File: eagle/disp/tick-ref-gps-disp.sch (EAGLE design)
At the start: 51 parts, among them CN1 1PPS Out, CN2 ISP, CN3 RS232, CN4 Power In, CN5 Serial Program, U1 ATMEGA168-AU, U2 AS1115, U3 MAX232, U4 LM2931_FIXED, X1 16MHz

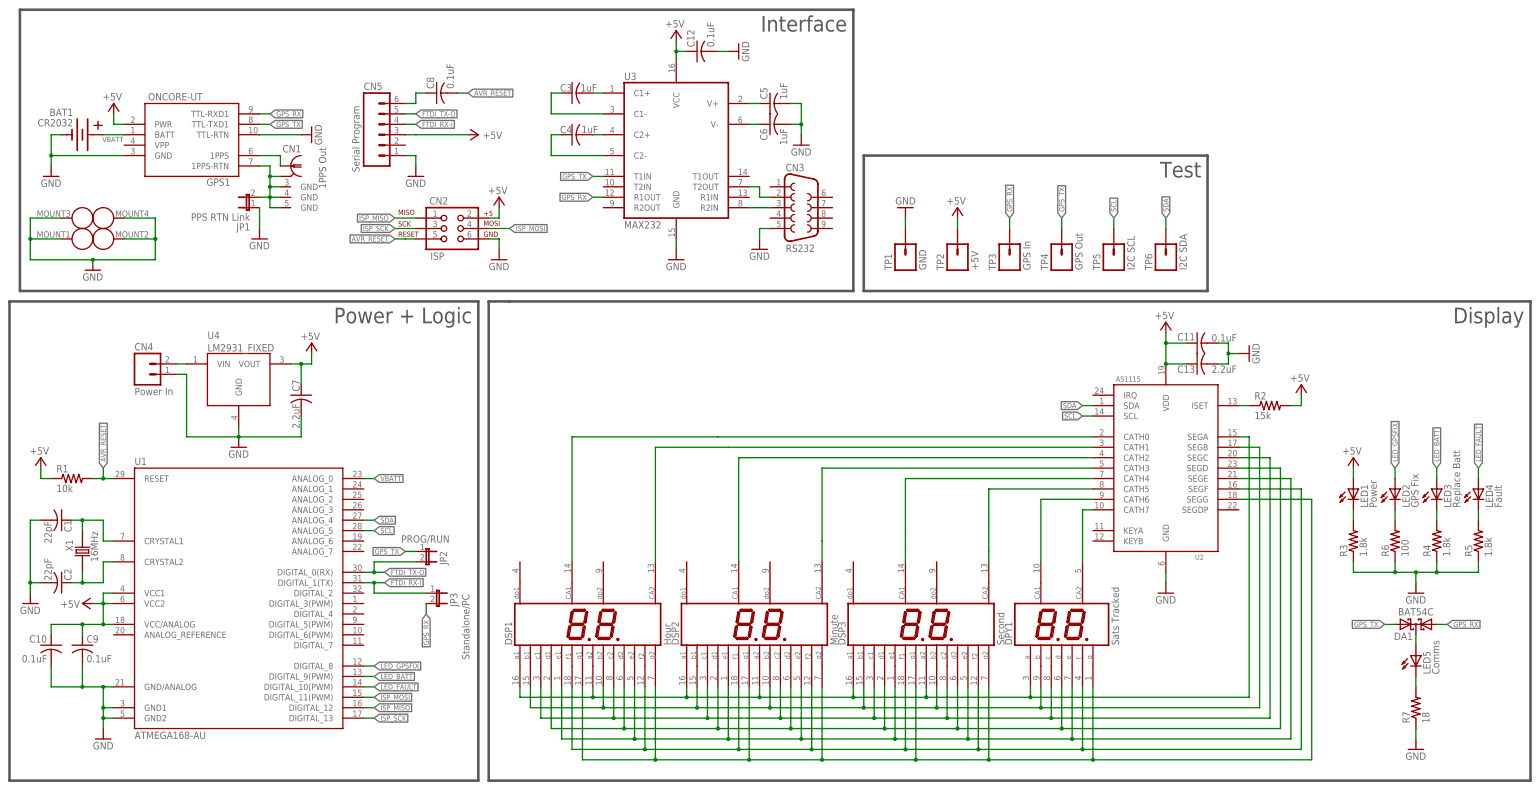
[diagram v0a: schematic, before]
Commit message: Display board schematic and layout electrically done, still need to figure out mechanical design and finalize this, plus run checklists.
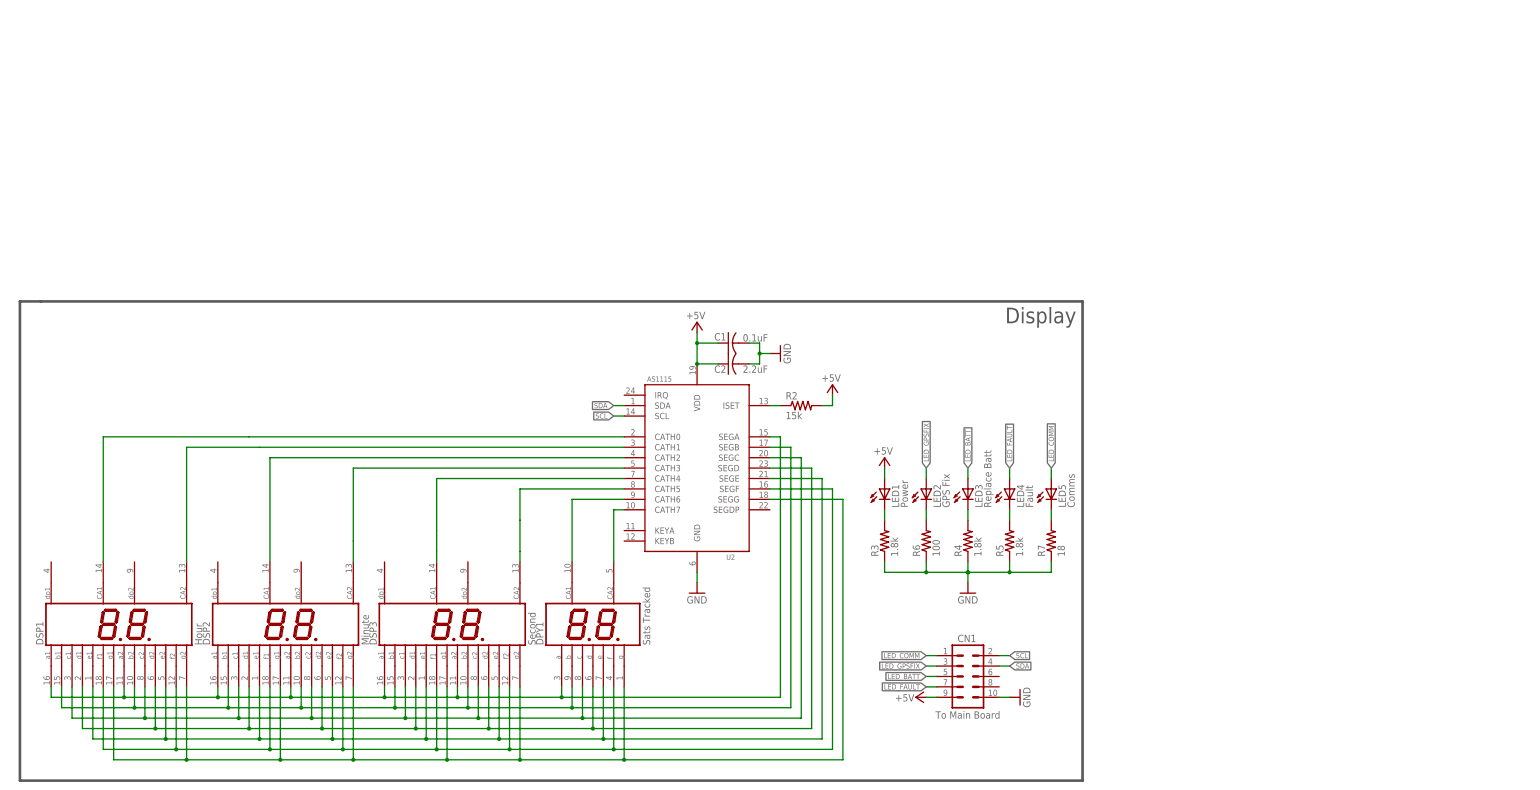
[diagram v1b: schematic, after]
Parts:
- removed BAT1: CR2032, con-sen:CR2032
- removed C10, C11, C12, C8, C9: 0.1uF, rcl:C-USC0603
- removed C13, C7: 2.2uF, rcl:C-USC0805
- removed C3, C4, C5, C6: 1uF, rcl:C-USC0603
- removed CN2: ISP, SparkFun:AVR_SPI_PRG_62X3_LOCK
- removed CN3: RS232, con-subd:F09VP
- removed CN4: Power In, SparkFun:M02POLAR_LOCK
- removed CN5: Serial Program, SparkFun:M06LOCK
- removed DA1: BAT54C, diode:BAT54C
- removed GPS1: ONCORE-UT, motorola-sen:ONCORE-UT
- removed JP1: PPS RTN Link, SparkFun:JUMPER-2SMD-NO
- removed JP2: PROG/RUN, SparkFun:JUMPER-2PTH_LOCK
- removed JP3: Standalone/PC, SparkFun:JUMPER-2SMD-NO
- removed R1: 10k, rcl:R-US_R0603
- removed TP1: GND, SparkFun:M01PTH
- removed TP2: +5V, SparkFun:M01PTH
- removed TP3: GPS In, SparkFun:M01PTH
- removed TP4: GPS Out, SparkFun:M01PTH
- removed TP5: I2C SCL, SparkFun:M01PTH
- removed TP6: I2C SDA, SparkFun:M01PTH
- removed U1: ATMEGA168-AU, Arduino-AVR:ATMEGA168-AU
- removed U3: MAX232, SparkFun-DigitalIC:MAX232SOIC16
- removed U4: LM2931_FIXED, SparkFun-PowerIC:LM2931_FIXED
- removed X1: 16MHz, crystal-sen:NX5032GA
- C1: value 22pF -> 0.1uF
- C2: value 22pF -> 2.2uF; device rcl:C-USC0603 -> rcl:C-USC0805
- CN1: value 1PPS Out -> To Main Board; device con-coax:B35N57 -> SparkFun-Connectors:M05X2PTH
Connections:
- removed net 1PPS: CN1G$1.1, GPS1G$1.1PPS
- removed net 1PPS_RTN: CN1G$1.GND, CN1G2.GND, CN1G3.GND, CN1G4.GND, GPS1G$1.1PPS-RTN, JP1.2
- removed net AVR_RESET: C8.2, CN2.5, R1.2, U1.RESET
- removed net FTDI_RTS: C8.1, CN5.6
- removed net FTDI_RX-I: CN5.4, JP3.1, U1.DIGITAL_1(TX)
- removed net FTDI_TX-O: CN5.5, JP2.2, U1.DIGITAL_0(RX)
- removed net GPS_RX: DA1.A1, GPS1G$1.TTL-RXD1, JP3.2, TP3.1, U3.R1OUT
- removed net GPS_RX_HV: CN3.3, U3.R2IN
- removed net GPS_TX: DA1.A2, GPS1G$1.TTL-TXD1, JP2.1, TP4.1, U3.T1IN
- removed net GPS_TX_HV: CN3.2, U3.T2OUT
- removed net ISP_MISO: CN2.1, U1.DIGITAL_12
- removed net ISP_MOSI: CN2.4, U1.DIGITAL_11(PWM)
- removed net ISP_SCK: CN2.3, U1.DIGITAL_13
- removed net LED5_D: DA1.CC, LED5.A
- removed net MAX232-C1+: C3.2, U3.C1+
- removed net MAX232-C1-: C3.1, U3.C1-
- removed net MAX232-C2+: C4.2, U3.C2+
- removed net MAX232-C2-: C4.1, U3.C2-
- removed net MAX232-V+: C5.1, U3.V+
- removed net MAX232-V-: C6.1, U3.V-
- removed net VBATT: BAT1.+2, GPS1G$1.BATT, U1.ANALOG_0
- removed net VIN: CN4.2, U4.VIN
- removed net XTAL1: C1.1, U1.CRYSTAL1, X1.2
- removed net XTAL2: C2.1, U1.CRYSTAL2, X1.1
- new net LED_COMM: CN1.1, LED5.A
- net +5V: now also C1.1, C2.1, CN1.9; no longer C10.1, C11.1, C12.1, C13.1, C7.1, C9.1, CN2.2, CN5.3, GPS1G$1.PWR, R1.1, TP2.1, U1.VCC/ANALOG, U1.VCC1, U1.VCC2, U3.VCC, U4.VOUT
- net GND: now also CN1.10; no longer BAT1.-1, C10.2, C11.2, C12.2, C13.2, C5.2, C6.2, C7.2, C9.2, CN2.6, CN3.5, CN4.1, CN5.1, GPS1G$1.GND, GPS1G$1.TTL-RTN, GPS1G$2.MOUNTHOLE1, GPS1G$2.MOUNTHOLE2, GPS1G$2.MOUNTHOLE3, GPS1G$2.MOUNTHOLE4, JP1.1, TP1.1, U1.GND/ANALOG, U1.GND1, U1.GND2, U3.GND, U4.GND
- net LED_BATT: now also CN1.5; no longer U1.DIGITAL_9(PWM)
- net LED_FAULT: now also CN1.7; no longer U1.DIGITAL_10(PWM)
- net LED_GPSFIX: now also CN1.3; no longer U1.DIGITAL_8
- net SCL: now also CN1.2; no longer TP5.1, U1.ANALOG_5
- net SDA: now also CN1.4; no longer TP6.1, U1.ANALOG_4
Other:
- note removed: "Interface"
- note removed: "Power + Logic"
- note removed: "Test"
- moved on the sheet: C1, C2, DPY1, DSP1, DSP2, DSP3, LED1, LED2, LED3, LED4, LED5, R2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

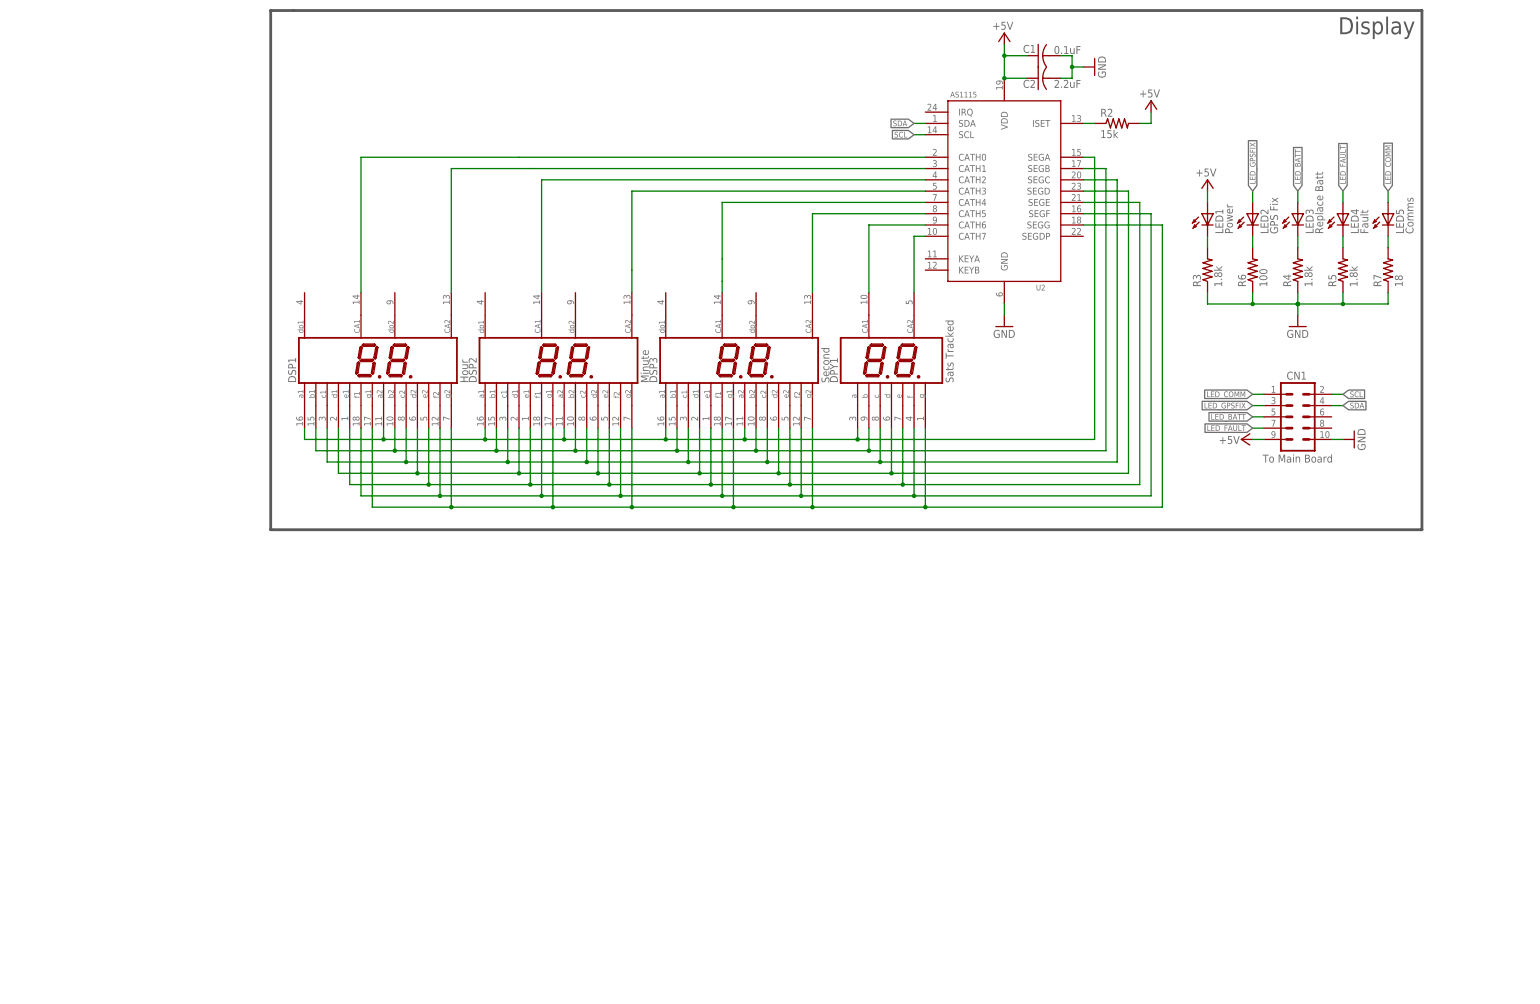
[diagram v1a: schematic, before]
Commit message: Schematic done for rev003 of the DISP board, 20 airwires left.
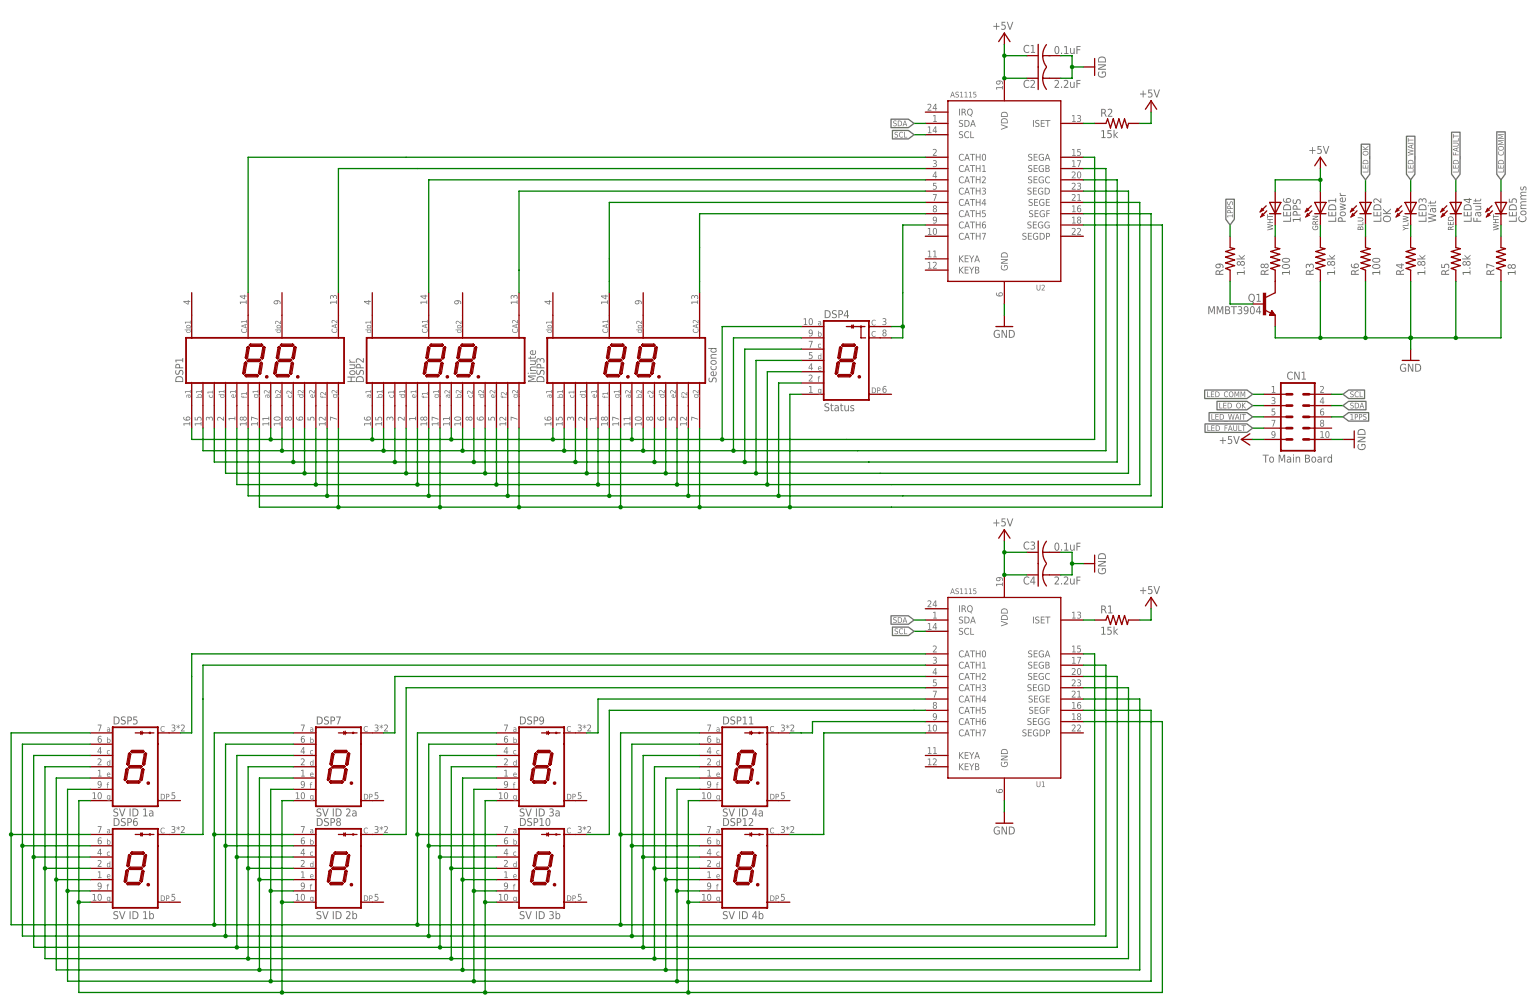
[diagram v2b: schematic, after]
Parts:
- removed DPY1: Sats Tracked, led-sen:LUMEX-LDD-F302NI
- added C3: 0.1uF, rcl:C-USC0603
- added C4: 2.2uF, rcl:C-USC0805
- added DSP10: SV ID 3b, led-sen:KINGBRIGHT-ACSC02
- added DSP11: SV ID 4a, led-sen:KINGBRIGHT-ACSC02
- added DSP12: SV ID 4b, led-sen:KINGBRIGHT-ACSC02
- added DSP4: Status, led-7-segment:S4301B
- added DSP5: SV ID 1a, led-sen:KINGBRIGHT-ACSC02
- added DSP6: SV ID 1b, led-sen:KINGBRIGHT-ACSC02
- added DSP7: SV ID 2a, led-sen:KINGBRIGHT-ACSC02
- added DSP8: SV ID 2b, led-sen:KINGBRIGHT-ACSC02
- added DSP9: SV ID 3a, led-sen:KINGBRIGHT-ACSC02
- added LED6: 1PPS, led:LED5MM
- added Q1: MMBT3904, SparkFun:TRANSISTOR_NPNSOT23
- added R1: 15k, rcl:R-US_R0603
- added R8: 100, rcl:R-US_R0603
- added R9: 1.8k, rcl:R-US_R0603
- added U1: AS1115, austria-sen:AS1115
- LED2: value GPS Fix -> OK
- LED3: value Replace Batt -> Wait
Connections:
- net LED_BATT renamed LED_WAIT
- net LED_GPSFIX renamed LED_OK
- removed net CATH_SATS_LS: DPY1.CA2, U2.CATH7
- removed net LED_SEG_A: DPY1.A, DSP1.A1, DSP1.A2, DSP2.A1, DSP2.A2, DSP3.A1, DSP3.A2, U2.SEGA
- removed net LED_SEG_B: DPY1.B, DSP1.B1, DSP1.B2, DSP2.B1, DSP2.B2, DSP3.B1, DSP3.B2, U2.SEGB
- removed net LED_SEG_C: DPY1.C, DSP1.C1, DSP1.C2, DSP2.C1, DSP2.C2, DSP3.C1, DSP3.C2, U2.SEGC
- removed net LED_SEG_D: DPY1.D, DSP1.D1, DSP1.D2, DSP2.D1, DSP2.D2, DSP3.D1, DSP3.D2, U2.SEGD
- removed net LED_SEG_E: DPY1.E, DSP1.E1, DSP1.E2, DSP2.E1, DSP2.E2, DSP3.E1, DSP3.E2, U2.SEGE
- removed net LED_SEG_F: DPY1.F, DSP1.F1, DSP1.F2, DSP2.F1, DSP2.F2, DSP3.F1, DSP3.F2, U2.SEGF
- removed net LED_SEG_G: DPY1.G, DSP1.G1, DSP1.G2, DSP2.G1, DSP2.G2, DSP3.G1, DSP3.G2, U2.SEGG
- new net 1PPS: CN1.6, R9.2
- new net 1PPS_Q: Q1.B, R9.1
- new net DSP10-C: DSP10.CATH, U1.CATH5
- new net DSP11-C: DSP11.CATH, U1.CATH6
- new net DSP12-C: DSP12.CATH, U1.CATH7
- new net DSP5-C: DSP5.CATH, U1.CATH0
- new net DSP6-C: DSP6.CATH, U1.CATH1
- new net DSP7-C: DSP7.CATH, U1.CATH2
- new net DSP8-C: DSP8.CATH, U1.CATH3
- new net DSP9-C: DSP9.CATH, U1.CATH4
- new net DSPA_SEG_A: DSP1.A1, DSP1.A2, DSP2.A1, DSP2.A2, DSP3.A1, DSP3.A2, DSP4.A, U2.SEGA
- new net DSPA_SEG_B: DSP1.B1, DSP1.B2, DSP2.B1, DSP2.B2, DSP3.B1, DSP3.B2, DSP4.B, U2.SEGB
- new net DSPA_SEG_C: DSP1.C1, DSP1.C2, DSP2.C1, DSP2.C2, DSP3.C1, DSP3.C2, DSP4.C, U2.SEGC
- new net DSPA_SEG_D: DSP1.D1, DSP1.D2, DSP2.D1, DSP2.D2, DSP3.D1, DSP3.D2, DSP4.D, U2.SEGD
- new net DSPA_SEG_E: DSP1.E1, DSP1.E2, DSP2.E1, DSP2.E2, DSP3.E1, DSP3.E2, DSP4.E, U2.SEGE
- new net DSPA_SEG_F: DSP1.F1, DSP1.F2, DSP2.F1, DSP2.F2, DSP3.F1, DSP3.F2, DSP4.F, U2.SEGF
- new net DSPA_SEG_G: DSP1.G1, DSP1.G2, DSP2.G1, DSP2.G2, DSP3.G1, DSP3.G2, DSP4.G, U2.SEGG
- new net DSPB_SEG_A: DSP10.A, DSP11.A, DSP12.A, DSP5.A, DSP6.A, DSP7.A, DSP8.A, DSP9.A, U1.SEGA
- new net DSPB_SEG_B: DSP10.B, DSP11.B, DSP12.B, DSP5.B, DSP6.B, DSP7.B, DSP8.B, DSP9.B, U1.SEGB
- new net DSPB_SEG_C: DSP10.C, DSP11.C, DSP12.C, DSP5.C, DSP6.C, DSP7.C, DSP8.C, DSP9.C, U1.SEGC
- new net DSPB_SEG_D: DSP10.D, DSP11.D, DSP12.D, DSP5.D, DSP6.D, DSP7.D, DSP8.D, DSP9.D, U1.SEGD
- new net DSPB_SEG_E: DSP10.E, DSP11.E, DSP12.E, DSP5.E, DSP6.E, DSP7.E, DSP8.E, DSP9.E, U1.SEGE
- new net DSPB_SEG_F: DSP10.F, DSP11.F, DSP12.F, DSP5.F, DSP6.F, DSP7.F, DSP8.F, DSP9.F, U1.SEGF
- new net DSPB_SEG_G: DSP10.G, DSP11.G, DSP12.G, DSP5.G, DSP6.G, DSP7.G, DSP8.G, DSP9.G, U1.SEGG
- new net LED6_R: LED6.C, R8.2
- new net LED_ISET1: R1.1, U1.ISET
- new net N$1: Q1.C, R8.1
- net +5V: now also C3.1, C4.1, LED6.A, R1.2, U1.VDD
- net CATH_SATS_MS: now also DSP4.C@1, DSP4.C@2; no longer DPY1.CA1
- net GND: now also C3.2, C4.2, Q1.E, U1.GND
- net SCL: now also U1.SCL
- net SDA: now also U1.SDA
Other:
- note added: "BLU"
- note added: "GRN"
- note added: "RED"
- note added: "WHT"
- note added: "YLW"
- note removed: "Display"
- moved on the sheet: DSP1, DSP2, DSP3, LED1, LED2, LED3, LED4, LED5, R3, R4, R5, R6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

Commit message: Finally got around to measuring the actual enclosure, made the board the final width, switched to larger time displays, and rerouted for this. Still have to rearrange silk and make board slightly less tall to fit.
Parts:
- DSP1, DSP2, DSP3: device display-hp:HD-K121 -> led-sen:LUMEX-LDD-C81XRI
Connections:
- net CATH_HOUR_LS: now also DSP1.CATH2; no longer DSP1.CA2
- net CATH_HOUR_MS: now also DSP1.CATH1; no longer DSP1.CA1
- net CATH_MIN_LS: now also DSP2.CATH2; no longer DSP2.CA2
- net CATH_MIN_MS: now also DSP2.CATH1; no longer DSP2.CA1
- net CATH_SEC_LS: now also DSP3.CATH2; no longer DSP3.CA2
- net CATH_SEC_MS: now also DSP3.CATH1; no longer DSP3.CA1
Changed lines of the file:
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@@
 <part name="P+5" library="supply1" deviceset="+5V" device=""/>
 <part name="GND7" library="supply1" deviceset="GND" device=""/>
-<part name="DSP1" library="display-hp" deviceset="HD-K121" device="" value="Hour"/>
-<part name="DSP2" library="display-hp" deviceset="HD-K121" device="" value="Minute"/>
-<part name="DSP3" library="display-hp" deviceset="HD-K121" device="" value="Second"/>
+<part name="DSP1" library="led-sen" deviceset="LUMEX-LDD-C81XRI" device="" value="Hour"/>
+<part name="DSP2" library="led-sen" deviceset="LUMEX-LDD-C81XRI" device="" value="Minute"/>
+<part name="DSP3" library="led-sen" deviceset="LUMEX-LDD-C81XRI" device="" value="Second"/>
 <part name="R2" library="rcl" deviceset="R-US_" device="R0603" value="15k"/>
 <part name="P+6" library="supply1" deviceset="+5V" device=""/>
@@
 <wire x1="147.32" y1="83.82" x2="30.48" y2="83.82" width="0.1524" layer="91"/>
 <wire x1="30.48" y1="83.82" x2="-5.08" y2="83.82" width="0.1524" layer="91"/>
-<pinref part="DSP1" gate="R" pin="CA1"/>
+<pinref part="DSP1" gate="R" pin="CATH1"/>
 <wire x1="-5.08" y1="53.34" x2="-5.08" y2="83.82" width="0.1524" layer="91"/>
 </segment>
@@
 <net name="CATH_MIN_MS" class="0">
 <segment>
-<pinref part="DSP2" gate="R" pin="CA1"/>
+<pinref part="DSP2" gate="R" pin="CATH1"/>
 <wire x1="35.56" y1="53.34" x2="35.56" y2="78.74" width="0.1524" layer="91"/>
 <pinref part="U2" gate="G$1" pin="CATH2"/>
@@
 <net name="CATH_MIN_LS" class="0">
 <segment>
-<pinref part="DSP2" gate="R" pin="CA2"/>
+<pinref part="DSP2" gate="R" pin="CATH2"/>
 <wire x1="55.88" y1="58.42" x2="55.88" y2="53.34" width="0.1524" layer="91"/>
 <pinref part="U2" gate="G$1" pin="CATH3"/>
@@
 <net name="CATH_SEC_MS" class="0">
 <segment>
-<pinref part="DSP3" gate="R" pin="CA1"/>
+<pinref part="DSP3" gate="R" pin="CATH1"/>
 <wire x1="76.2" y1="53.34" x2="76.2" y2="55.88" width="0.1524" layer="91"/>
 <pinref part="U2" gate="G$1" pin="CATH4"/>
@@
 <net name="CATH_SEC_LS" class="0">
 <segment>
-<pinref part="DSP3" gate="R" pin="CA2"/>
+<pinref part="DSP3" gate="R" pin="CATH2"/>
 <wire x1="96.52" y1="55.88" x2="96.52" y2="53.34" width="0.1524" layer="91"/>
 <wire x1="96.52" y1="55.88" x2="96.52" y2="63.5" width="0.1524" layer="91"/>
@@
 <net name="CATH_HOUR_LS" class="0">
 <segment>
-<pinref part="DSP1" gate="R" pin="CA2"/>
+<pinref part="DSP1" gate="R" pin="CATH2"/>
 <wire x1="15.24" y1="53.34" x2="15.24" y2="81.28" width="0.1524" layer="91"/>
 <pinref part="U2" gate="G$1" pin="CATH1"/>
